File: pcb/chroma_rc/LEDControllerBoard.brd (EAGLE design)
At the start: 33.3 x 46 mm, 38 parts

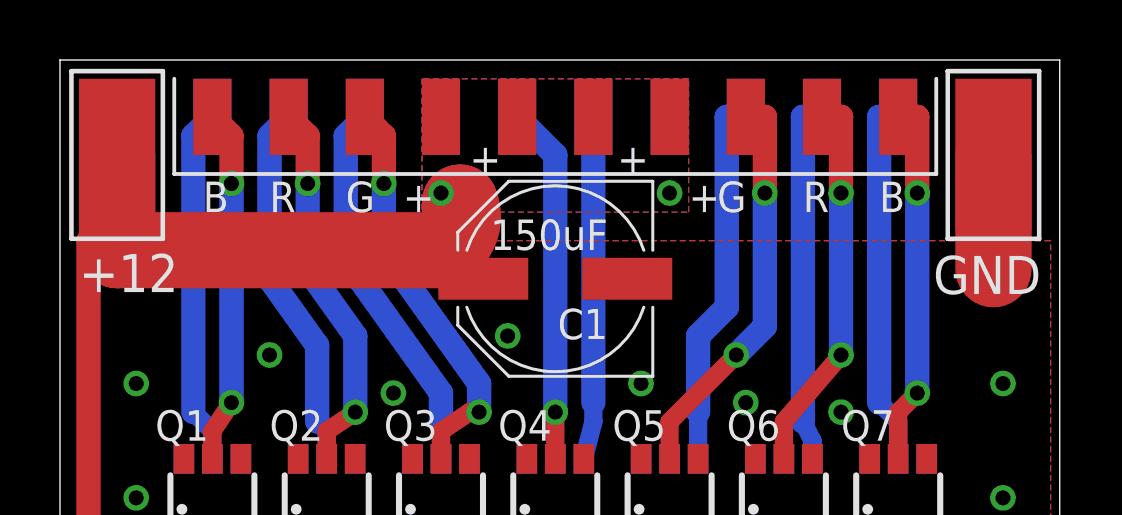
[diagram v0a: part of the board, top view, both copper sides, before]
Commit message: PCB v1.3.  Added second set of power pads on the bottom.
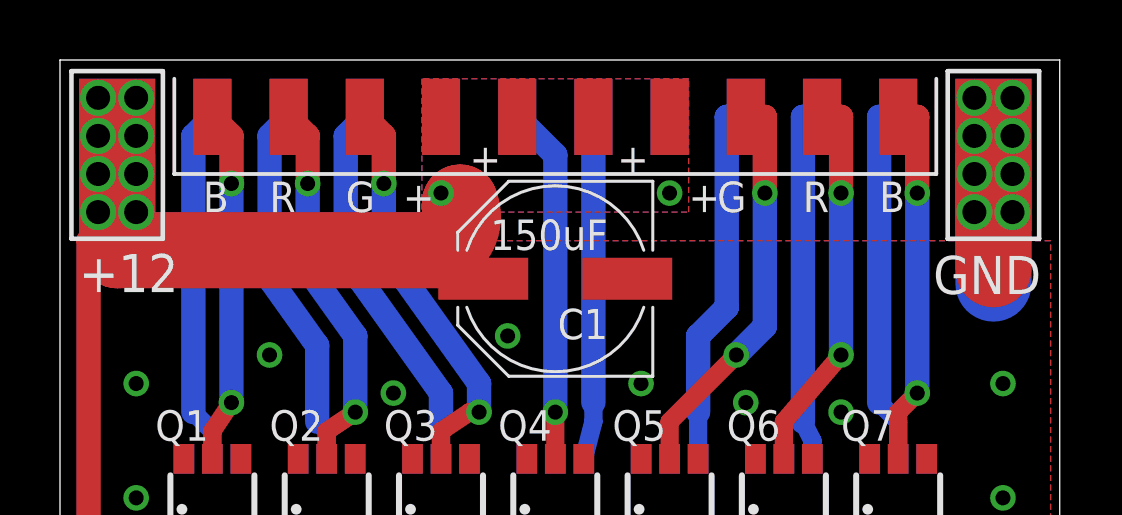
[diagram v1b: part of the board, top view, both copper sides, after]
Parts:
- added +1, GND1: WIREPADSMD5-2,5, wirepad:5-2,5
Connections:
- net +12V: now also +1.1
- net GND: now also GND1.1
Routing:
- net GND: track 3.81 -> 24.6 mm, vias 21 -> 29
- net +12V: track 41.1 -> 52.5 mm, vias 3 -> 11
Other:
- board text added: "Chroma-RC"
- board text added: "Clough v1.3"
- board text removed: "Clough v1.2"
- board text removed: "RGB LED Controller"
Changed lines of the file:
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@@
 <layer number="18" name="Vias" color="2" fill="1" visible="yes" active="yes"/>
 <layer number="19" name="Unrouted" color="6" fill="1" visible="yes" active="yes"/>
-<layer number="20" name="Dimension" color="15" fill="1" visible="yes" active="yes"/>
+<layer number="20" name="Dimension" color="15" fill="1" visible="no" active="yes"/>
 <layer number="21" name="tPlace" color="7" fill="1" visible="yes" active="yes"/>
 <layer number="22" name="bPlace" color="7" fill="1" visible="yes" active="yes"/>
@@
 <text x="16.98625" y="45.085" size="1.016" layer="26" rot="MR0">X</text>
 <text x="19.52625" y="45.085" size="1.016" layer="26" rot="MR0">Y</text>
-<text x="33.3375" y="23.1775" size="1.016" layer="26" rot="MR270">RGB LED Controller</text>
-<text x="31.75" y="20.6375" size="1.016" layer="26" rot="MR270">Clough v1.2</text>
+<text x="33.3375" y="20.6375" size="1.016" layer="26" rot="MR270">Chroma-RC</text>
+<text x="31.75" y="20.6375" size="1.016" layer="26" rot="MR270">Clough v1.3</text>
 </plain>
 <attributes>
@@
 <attribute name="VALUE" x="19.53" y="44.8375" size="1.016" layer="25" rot="R180"/>
 </element>
+<element name="+1" library="wirepad" package="5-2,5" value="WIREPADSMD5-2,5" x="3.175" y="46.99" smashed="yes" rot="MR0">
+<attribute name="VALUE" x="3.275" y="49.79" size="0.0254" layer="28" rot="MR0"/>
+</element>
+<element name="GND1" library="wirepad" package="5-2,5" value="WIREPADSMD5-2,5" x="32.385" y="46.99" smashed="yes" rot="MR180">
+<attribute name="VALUE" x="32.285" y="44.19" size="0.0254" layer="28" rot="MR180"/>
+</element>
 </elements>
 <signals>
@@
 <via x="27.305" y="38.4175" extent="1-16" drill="0.5"/>
 <via x="24.13" y="38.735" extent="1-16" drill="0.5"/>
+<contactref element="GND1" pad="1"/>
+<wire x1="32.385" y1="46.99" x2="31.75" y2="46.99" width="0.4064" layer="16"/>
+<wire x1="31.75" y1="46.99" x2="31.75" y2="47.625" width="0.4064" layer="16"/>
+<via x="31.75" y="48.895" extent="1-16" drill="0.8"/>
+<wire x1="31.75" y1="47.625" x2="31.75" y2="48.895" width="0.4064" layer="16"/>
+<wire x1="31.75" y1="48.895" x2="32.385" y2="48.895" width="0.4064" layer="1"/>
+<wire x1="32.385" y1="48.895" x2="32.385" y2="46.99" width="0.4064" layer="1"/>
+<via x="31.75" y="47.625" extent="1-16" drill="0.8"/>
+<via x="33.02" y="48.895" extent="1-16" drill="0.8"/>
+<via x="33.02" y="47.625" extent="1-16" drill="0.8"/>
+<via x="33.02" y="46.355" extent="1-16" drill="0.8"/>
+<via x="33.02" y="45.085" extent="1-16" drill="0.8"/>
+<via x="31.75" y="45.085" extent="1-16" drill="0.8"/>
+<via x="31.75" y="46.355" extent="1-16" drill="0.8"/>
+<wire x1="31.75" y1="46.99" x2="33.02" y2="46.99" width="0.4064" layer="1"/>
+<wire x1="33.02" y1="46.99" x2="33.02" y2="46.355" width="0.4064" layer="1"/>
+<wire x1="33.02" y1="45.085" x2="33.02" y2="44.45" width="0.4064" layer="1"/>
+<wire x1="33.02" y1="48.895" x2="31.75" y2="48.895" width="0.4064" layer="1"/>
+<wire x1="33.02" y1="47.625" x2="33.02" y2="46.99" width="0.4064" layer="1"/>
+<wire x1="33.02" y1="46.355" x2="33.02" y2="45.085" width="0.4064" layer="1"/>
+<wire x1="33.02" y1="45.085" x2="31.75" y2="45.085" width="0.4064" layer="1"/>
+<wire x1="31.75" y1="45.085" x2="31.75" y2="46.355" width="0.4064" layer="1"/>
+<wire x1="31.75" y1="46.355" x2="31.75" y2="46.99" width="0.4064" layer="1"/>
+<wire x1="31.75" y1="46.355" x2="31.75" y2="48.895" width="0.4064" layer="1"/>
+<wire x1="32.385" y1="46.99" x2="32.385" y2="42.70375" width="2.54" layer="16"/>
 </signal>
 <signal name="N$1">
@@
 <wire x1="15.38" y1="42.8625" x2="15.24" y2="42.8625" width="1.27" layer="1"/>
 <wire x1="15.24" y1="42.8625" x2="13.97" y2="43.815" width="1.27" layer="1"/>
+<contactref element="+1" pad="1"/>
+<wire x1="3.175" y1="46.99" x2="2.54" y2="46.99" width="0.4064" layer="1"/>
+<wire x1="2.54" y1="46.99" x2="2.54" y2="47.625" width="0.4064" layer="1"/>
+<via x="2.54" y="48.895" extent="1-16" drill="0.8"/>
+<wire x1="2.54" y1="47.625" x2="2.54" y2="48.895" width="0.4064" layer="1"/>
+<wire x1="2.54" y1="48.895" x2="3.175" y2="48.895" width="0.4064" layer="16"/>
+<wire x1="3.175" y1="48.895" x2="3.175" y2="46.99" width="0.4064" layer="16"/>
+<via x="2.54" y="47.625" extent="1-16" drill="0.8"/>
+<via x="3.81" y="48.895" extent="1-16" drill="0.8"/>
+<via x="3.81" y="47.625" extent="1-16" drill="0.8"/>
+<via x="3.81" y="46.355" extent="1-16" drill="0.8"/>
+<via x="2.54" y="46.355" extent="1-16" drill="0.8"/>
+<via x="2.54" y="45.085" extent="1-16" drill="0.8"/>
+<via x="3.81" y="45.085" extent="1-16" drill="0.8"/>
+<wire x1="3.81" y1="48.895" x2="3.81" y2="47.625" width="0.4064" layer="1"/>
+<wire x1="3.81" y1="47.625" x2="3.81" y2="46.355" width="0.4064" layer="1"/>
+<wire x1="3.81" y1="46.355" x2="3.81" y2="45.085" width="0.4064" layer="1"/>
+<wire x1="3.81" y1="46.355" x2="2.54" y2="46.355" width="0.4064" layer="1"/>
+<wire x1="2.54" y1="46.355" x2="2.54" y2="45.085" width="0.4064" layer="1"/>
+<wire x1="3.175" y1="48.895" x2="3.81" y2="48.895" width="0" layer="19" extent="16-16"/>
 </signal>
 <signal name="N$3">
